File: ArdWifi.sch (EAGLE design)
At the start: 17 parts, among them Q1 8/16/20MHz, U1 ATMEGA328, U2 MIC5205

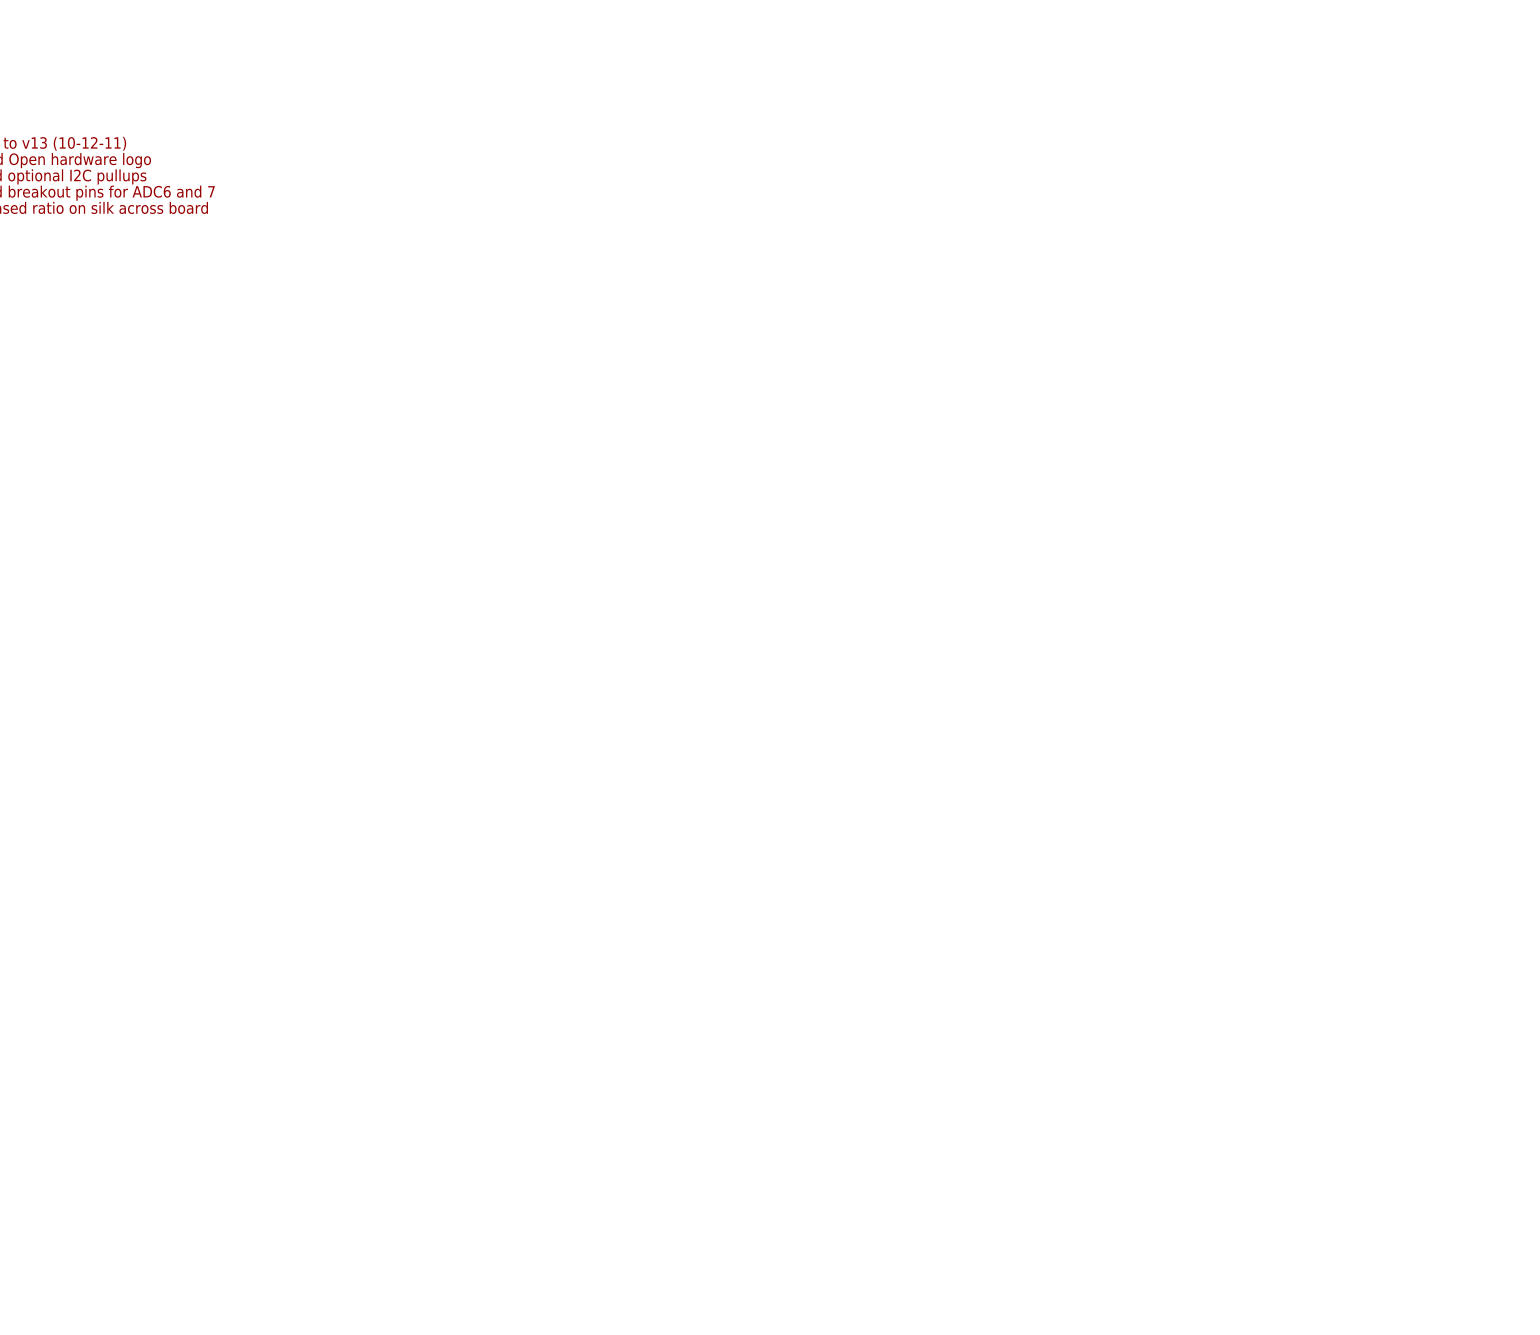
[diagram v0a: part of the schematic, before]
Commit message: add wifi chip
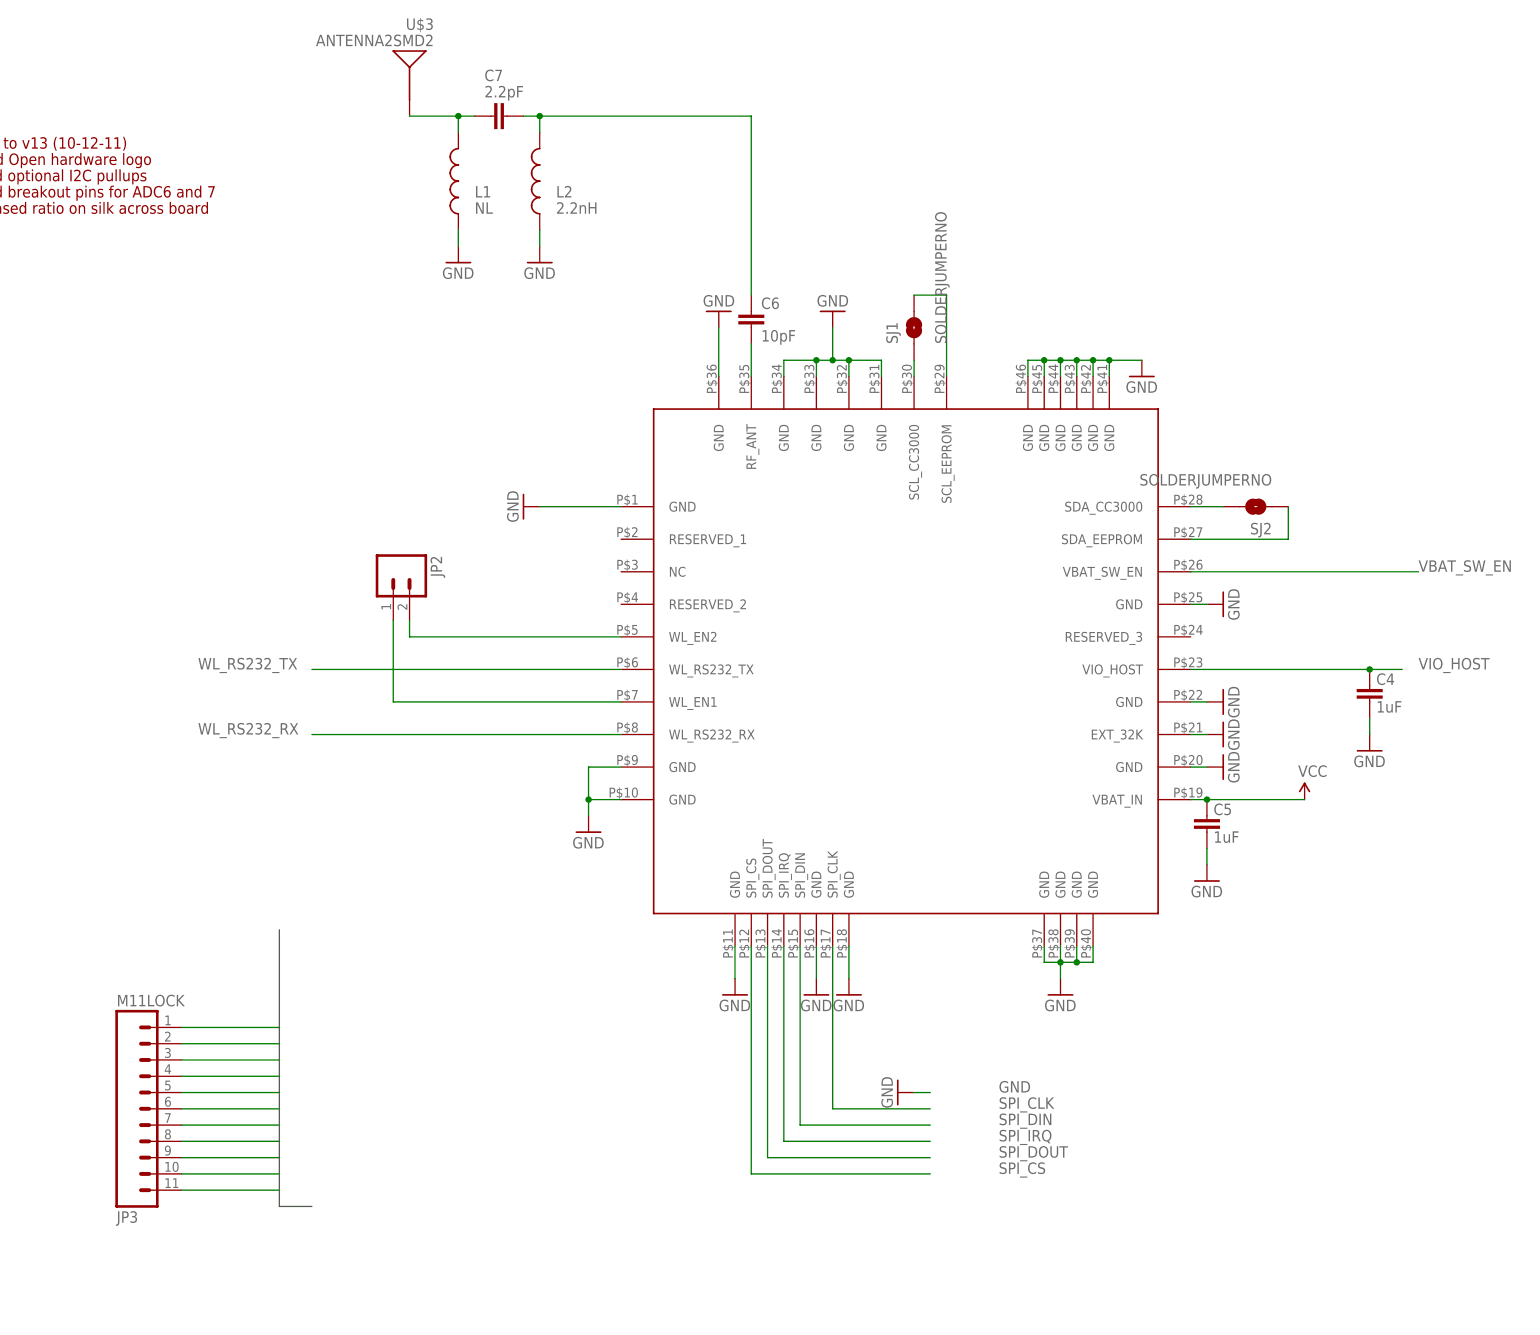
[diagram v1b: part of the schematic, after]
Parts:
- added C4, C5: 1uF, SparkFun:CAP0402-CAP
- added C6: 10pF, SparkFun:CAP0402-CAP
- added C7: 2.2pF, SparkFun:CAP0402-CAP
- added JP2: (no value), SparkFun:M02LOCK
- added JP3: M11LOCK, SparkFun:M11LOCK
- added L1: NL, SparkFun:INDUCTOR0402
- added L2: 2.2nH, SparkFun:INDUCTOR0402
- added SJ1, SJ2: SOLDERJUMPERNO, SparkFun:SOLDERJUMPERNO
- added U$1: CC3000, centerblack_engineering:CC3000
- added U$3: ANTENNA2SMD2, SparkFun:ANTENNA2SMD2
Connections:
- new net 3.3V: C5.2, JP3.11, U$1.VBAT_IN
- new net N$10: C6.1, C7.2, L2.2
- new net N$13: C6.2, U$1.RF_ANT
- new net N$14: SJ1.1, U$1.SCL_CC3000
- new net N$15: C7.1, L1.2, U$3.SIGNAL
- new net N$16: SJ1.2, U$1.SCL_EEPROM
- new net N$17: SJ2.2, U$1.SDA_CC3000
- new net N$18: SJ2.1, U$1.SDA_EEPROM
- new net SPI_CLK: JP3.7, U$1.SPI_CLK
- new net SPI_CS: JP3.3, U$1.SPI_CS
- new net SPI_DIN: JP3.6, U$1.SPI_DIN
- new net SPI_DOUT: JP3.4, U$1.SPI_DOUT
- new net SPI_IRQ: JP3.5, U$1.SPI_IRQ
- new net VBAT_SW_EN: JP3.9, U$1.VBAT_SW_EN
- new net VIO_HOST: C4.2, JP3.8, U$1.VIO_HOST
- new net WL_EN1: JP2.1, U$1.WL_EN1
- new net WL_EN2: JP2.2, U$1.WL_EN2
- new net WL_RS232_RX: JP3.2, U$1.WL_RS232_RX
- new net WL_RS232_TX: JP3.1, U$1.WL_RS232_TX
- net GND: now also C4.1, C5.1, JP3.10, L1.1, L2.1, U$1.EXT_32K, U$1.GND, U$1.GND@10, U$1.GND@11, U$1.GND@16, U$1.GND@18, U$1.GND@20, U$1.GND@22, U$1.GND@25, U$1.GND@31, U$1.GND@32, U$1.GND@33, U$1.GND@34, U$1.GND@36, U$1.GND@37, U$1.GND@38, U$1.GND@39, U$1.GND@40, U$1.GND@41, U$1.GND@42, U$1.GND@43, U$1.GND@44, U$1.GND@45, U$1.GND@46, U$1.GND@9

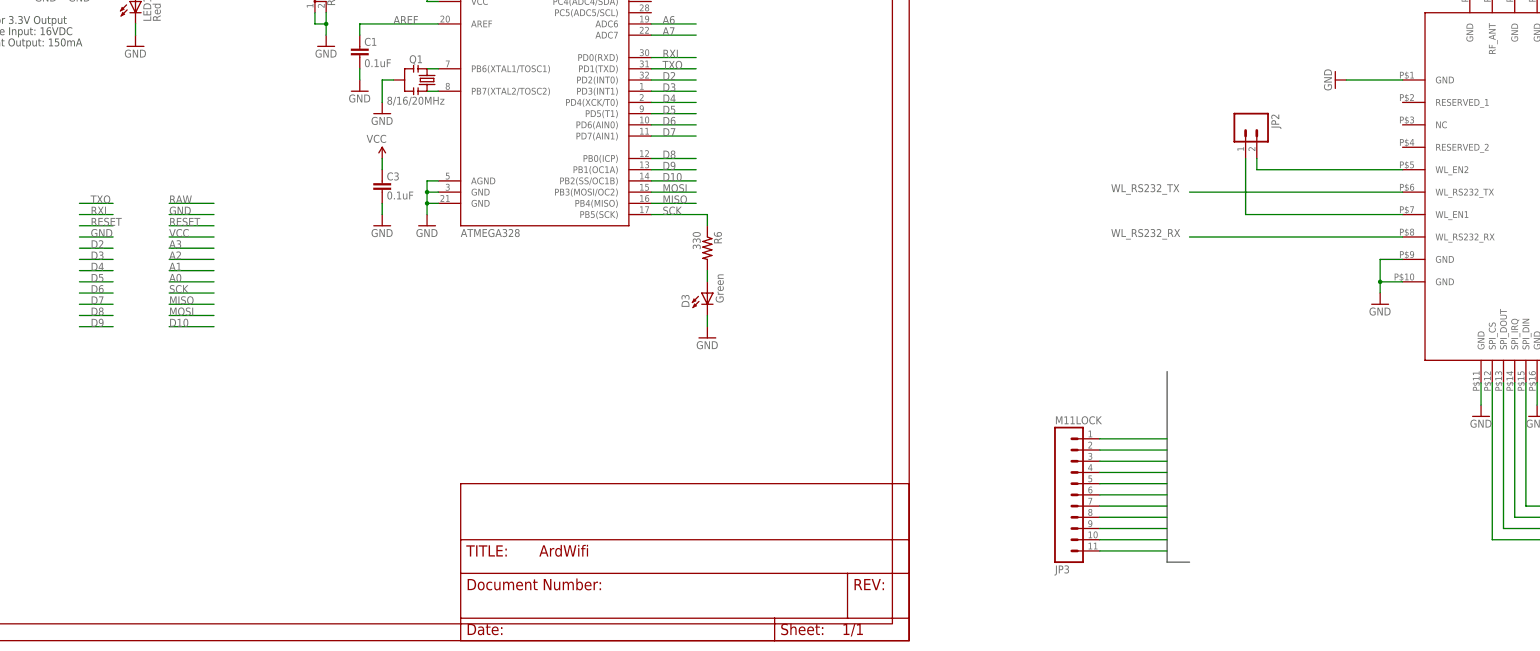
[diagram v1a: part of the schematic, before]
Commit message: connect wifi chip
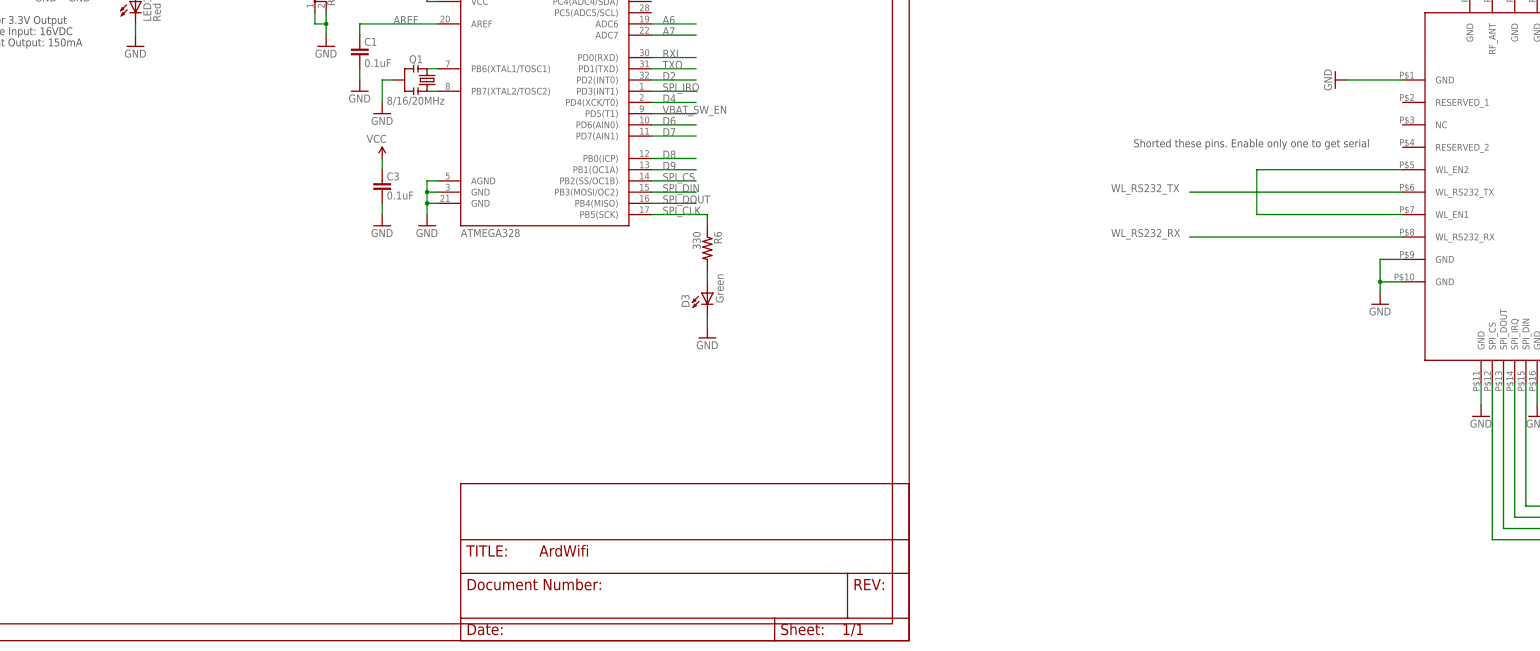
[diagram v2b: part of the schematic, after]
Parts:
- removed JP2: (no value), SparkFun:M02LOCK
- removed JP3: M11LOCK, SparkFun:M11LOCK
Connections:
- removed net 3.3V: C5.2, JP3.11, U$1.VBAT_IN
- removed net D10: U1.PB2(SS/OC1B)
- removed net D3: U1.PD3(INT1)
- removed net D5: U1.PD5(T1)
- removed net MISO: U1.PB4(MISO)
- removed net MOSI: U1.PB3(MOSI/OC2)
- removed net SCK: R6.1, U1.PB5(SCK)
- removed net WL_EN1: JP2.1, U$1.WL_EN1
- net GND: no longer JP3.10
- net SPI_CLK: now also R6.1, U1.PB5(SCK); no longer JP3.7
- net SPI_CS: now also U1.PB2(SS/OC1B); no longer JP3.3
- net SPI_DIN: now also U1.PB3(MOSI/OC2); no longer JP3.6
- net SPI_DOUT: now also U1.PB4(MISO); no longer JP3.4
- net SPI_IRQ: now also U1.PD3(INT1); no longer JP3.5
- net VBAT_SW_EN: now also U1.PD5(T1); no longer JP3.9
- net VCC: now also C5.2, U$1.VBAT_IN
- net VIO_HOST: no longer JP3.8
- net WL_EN2: now also U$1.WL_EN1; no longer JP2.2
- net WL_RS232_RX: no longer JP3.2
- net WL_RS232_TX: no longer JP3.1
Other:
- note added: "Shorted these pins. Enable only one to get serial"

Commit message: added lvl shifter
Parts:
- removed FRM1: (no value), Frames:LETTER
- removed SJ1, SJ2: SOLDERJUMPERNO, SparkFun:SOLDERJUMPERNO
- removed U2: MIC5205, SparkFun:V_REG_LDOSMD
- added R3: 10K, resistor:R-US_R0603
- added REG1: LDO_UA78M33, carrilib:LDO_UA78M33
- added U3: TXB0106, McLEng:TXB0106PWR
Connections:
- removed net N$14: SJ1.1, U$1.SCL_CC3000
- removed net N$17: SJ2.2, U$1.SDA_CC3000
- new net +3V3: R3.1, U3.VCCA
- new net N$114: R3.2, U3.OE
- net GND: now also REG1.G1, REG1.G2, U3.GND; no longer U2.GND
- net N$16: now also U$1.SCL_CC3000; no longer SJ1.2
- net N$18: now also U$1.SDA_CC3000; no longer SJ2.1
- net RAW: now also JP1.VCC, REG1.VI; no longer U2.EN, U2.IN
- net VCC: now also REG1.VO, U3.VCCB; no longer JP1.VCC, U2.OUT
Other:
- note added: "3.3V on the left and 5V on the right"
- note added: "3V3 Regulator"
- note added: "5V Input for Power and Serial communication"
- note added: "Arduino MPU"
- note added: "Atmega328P chip flashes with 16Mhz Arduino Firmware"
- note added: "CC3000 WiFi Module"
- note added: "Main Connector"
- note added: "SPI Level Shifter"
- note added: "TXB0104: 5V-3V3 Level Shifter for SPI"
- note added: "UA78M33: Max output 500mA"
- note added: "WiFi Module"
- note removed: "-Added Open hardware logo"
- note removed: "-added breakout pins for ADC6 and 7"
- note removed: "-added optional I2C pullups"
- note removed: "-increased ratio on silk across board"
- note removed: "Changes to v13 (10-12-11)"
- note removed: "Max Current Output: 150mA"
- note removed: "Max Voltage Input: 16VDC"
- note removed: "VCC = 5V or 3.3V Output"
- moved on the sheet: C1, C10, C13, C19, C2, C3, C4, C5, C6, C7, D3, JP1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
